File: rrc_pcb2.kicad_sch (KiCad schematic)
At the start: 15 parts, among them J1 Conn_01x02_Male-Connector, J2 Conn_01x03_Male-Connector, J3 digital logic connection, U1 iridium9602, U2 Teensy4.1, U3 BN220-GPS, U4 ICM-20948, U5 MS5611, U6 logo, U7 voltReg

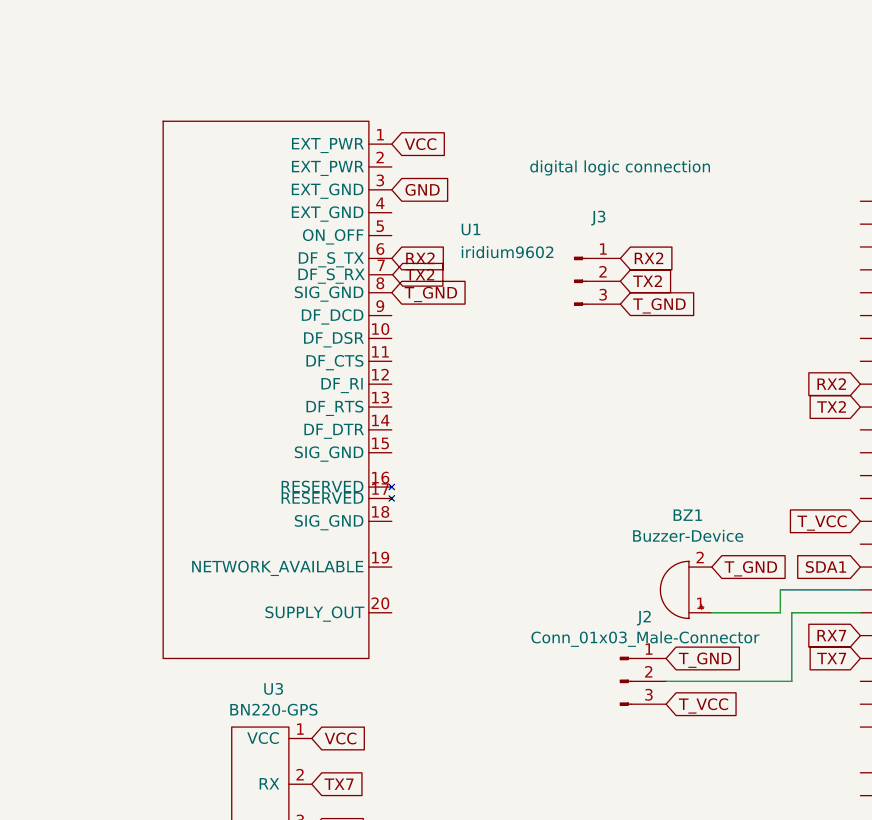
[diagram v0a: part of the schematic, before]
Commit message: tweaked srad main board
tweaked iridium footprints and volt reg footprints and added a back board just in case iridium doenst pan out; uses rfd900p instead.
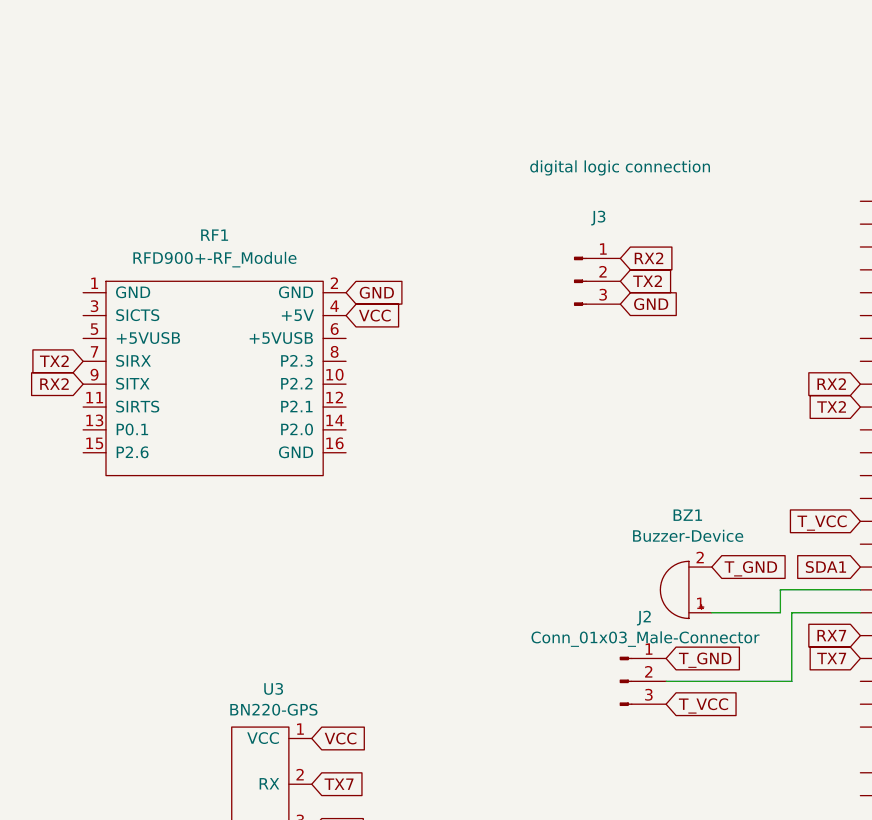
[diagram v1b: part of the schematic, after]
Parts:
- removed U1: iridium9602, iridium9602:iridium9602, symbol parts:iridium9602
- added RF1: RFD900+-RF_Module, rfd900+:RFD900+, symbol parts:RFD900+-RF_Module
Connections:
- net GND: now also J3.3 (Pin_3), RF1.2 (GND)
- net RX2: now also RF1.9 (SITX)
- net TX2: now also RF1.7 (SIRX)
- net T_GND: no longer J3.3 (Pin_3)
- net VCC: now also RF1.4 (+5V)
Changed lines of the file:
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@@
+    )
+  )
+  (global_label "GND" (shape input) (at 72.39 33.02 0) (fields_autoplaced)
+    (effects (font (size 1.27 1.27)) (justify left))
+    (property "Intersheet References" "${INTERSHEET_REFS}" (id 0) (at 0 -68.58 0)
+      (effects (font (size 1.27 1.27)) hide)
     )
   )
@@
     )
   )
-  (global_label "TX2" (shape input) (at 47.0887 29.7566 0) (fields_autoplaced)
-    (effects (font (size 1.27 1.27)) (justify left))
-    (property "Intersheet References" "${INTERSHEET_REFS}" (id 0) (at 52.7996 29.6772 0)
-      (effects (font (size 1.27 1.27)) (justify left) hide)
+  (global_label "TX2" (shape input) (at 12.7 39.37 180) (fields_autoplaced)
+    (effects (font (size 1.27 1.27)) (justify right))
+    (property "Intersheet References" "${INTERSHEET_REFS}" (id 0) (at 6.9891 39.4494 0)
+      (effects (font (size 1.27 1.27)) (justify right) hide)
     )
   )
@@
     )
   )
-  (global_label "VCC" (shape input) (at 46.99 15.24 0) (fields_autoplaced)
-    (effects (font (size 1.27 1.27)) (justify left))
-    (property "Intersheet References" "${INTERSHEET_REFS}" (id 0) (at -121.92 -113.03 0)
+  (global_label "VCC" (shape input) (at 41.91 34.29 0) (fields_autoplaced)
+    (effects (font (size 1.27 1.27)) (justify left))
+    (property "Intersheet References" "${INTERSHEET_REFS}" (id 0) (at -127 -93.98 0)
       (effects (font (size 1.27 1.27)) hide)
     )
@@
     )
   )
-  (global_label "RX2" (shape input) (at 46.99 27.94 0) (fields_autoplaced)
-    (effects (font (size 1.27 1.27)) (justify left))
-    (property "Intersheet References" "${INTERSHEET_REFS}" (id 0) (at 53.0032 27.8606 0)
-      (effects (font (size 1.27 1.27)) (justify left) hide)
+  (global_label "RX2" (shape input) (at 12.7 41.91 180) (fields_autoplaced)
+    (effects (font (size 1.27 1.27)) (justify right))
+    (property "Intersheet References" "${INTERSHEET_REFS}" (id 0) (at 6.6868 41.9894 0)
+      (effects (font (size 1.27 1.27)) (justify right) hide)
     )
   )
@@
     )
   )
-  (global_label "T_GND" (shape input) (at 46.99 31.75 0) (fields_autoplaced)
-    (effects (font (size 1.27 1.27)) (justify left))
-    (property "Intersheet References" "${INTERSHEET_REFS}" (id 0) (at -19.05 -13.97 0)
-      (effects (font (size 1.27 1.27)) hide)
-    )
-  )
   (global_label "T_GND" (shape input) (at 38.1 95.25 0) (fields_autoplaced)
     (effects (font (size 1.27 1.27)) (justify left))
@@
     )
   )
-  (global_label "T_GND" (shape input) (at 72.39 33.02 0) (fields_autoplaced)
-    (effects (font (size 1.27 1.27)) (justify left))
-    (property "Intersheet References" "${INTERSHEET_REFS}" (id 0) (at 6.35 -12.7 0)
-      (effects (font (size 1.27 1.27)) hide)
-    )
-  )
   (global_label "VCC" (shape input) (at 38.1 81.28 0) (fields_autoplaced)
     (effects (font (size 1.27 1.27)) (justify left))
@@
     )
   )
-  (global_label "GND" (shape input) (at 46.99 20.32 0) (fields_autoplaced)
-    (effects (font (size 1.27 1.27)) (justify left))
-    (property "Intersheet References" "${INTERSHEET_REFS}" (id 0) (at -25.4 -81.28 0)
+  (global_label "GND" (shape input) (at 41.91 31.75 0) (fields_autoplaced)
+    (effects (font (size 1.27 1.27)) (justify left))
+    (property "Intersheet References" "${INTERSHEET_REFS}" (id 0) (at -30.48 -69.85 0)
       (effects (font (size 1.27 1.27)) hide)
     )
@@
     (pin "23")
     (pin "24")
-    (pin "3")
-    (pin "4")
-    (pin "5")
-    (pin "6")
-    (pin "7")
-    (pin "8")
-    (pin "9")
-  )
-  (symbol (lib_id "parts:iridium9602") (at 34.29 21.59 0) (unit 1)
-    (in_bom yes) (on_board yes) (fields_autoplaced)
-    (property "Reference" "U1" (id 0) (at 54.61 24.7649 0)
-      (effects (font (size 1.27 1.27)) (justify left))
-    )
-    (property "Value" "iridium9602" (id 1) (at 54.61 27.3049 0)
-      (effects (font (size 1.27 1.27)) (justify left))
-    )
-    (property "Footprint" "iridium9602:iridium9602" (id 2) (at 34.29 21.59 0)
-      (effects (font (size 1.27 1.27)) hide)
-    )
-    (property "Datasheet" "" (id 3) (at 34.29 21.59 0)
-      (effects (font (size 1.27 1.27)) hide)
-    )
-    (pin "1")
-    (pin "10")
-    (pin "11")
-    (pin "12")
-    (pin "13")
-    (pin "14")
-    (pin "15")
-    (pin "16")
-    (pin "17")
-    (pin "18")
-    (pin "19")
-    (pin "2")
-    (pin "20")
     (pin "3")
     (pin "4")
@@
     (pin "4")
   )
+  (symbol (lib_id "parts:RFD900+-RF_Module") (at 19.05 31.75 0) (unit 1)
+    (in_bom yes) (on_board yes) (fields_autoplaced)
+    (property "Reference" "RF1" (id 0) (at 27.305 25.4 0))
+    (property "Value" "RFD900+-RF_Module" (id 1) (at 27.305 27.94 0))
+    (property "Footprint" "rfd900+:RFD900+" (id 2) (at 19.05 31.75 0)
+      (effects (font (size 1.27 1.27)) hide)
+    )
+    (property "Datasheet" "" (id 3) (at 19.05 31.75 0)
+      (effects (font (size 1.27 1.27)) hide)
+    )
+    (pin "1")
+    (pin "10")
+    (pin "11")
+    (pin "12")
+    (pin "13")
+    (pin "14")
+    (pin "15")
+    (pin "16")
+    (pin "2")
+    (pin "3")
+    (pin "4")
+    (pin "5")
+    (pin "6")
+    (pin "7")
+    (pin "8")
+    (pin "9")
+  )
   (sheet_instances
     (path "/" (page "1"))
@@
       (reference "R4") (unit 1) (value "R-Device") (footprint "Resistor_THT:R_Axial_DIN0207_L6.3mm_D2.5mm_P10.16mm_Horizontal")
     )
-    (path "/84f80ca1-29d4-4e34-8c20-e0b5bcec9cb7"
-      (reference "U1") (unit 1) (value "iridium9602") (footprint "iridium9602:iridium9602")
+    (path "/f8d3fd09-f76b-4951-941b-625c4e65f1c1"
+      (reference "RF1") (unit 1) (value "RFD900+-RF_Module") (footprint "rfd900+:RFD900+")
     )
     (path "/e2a4979b-162a-4acf-966e-29cd5e9f5e0d"

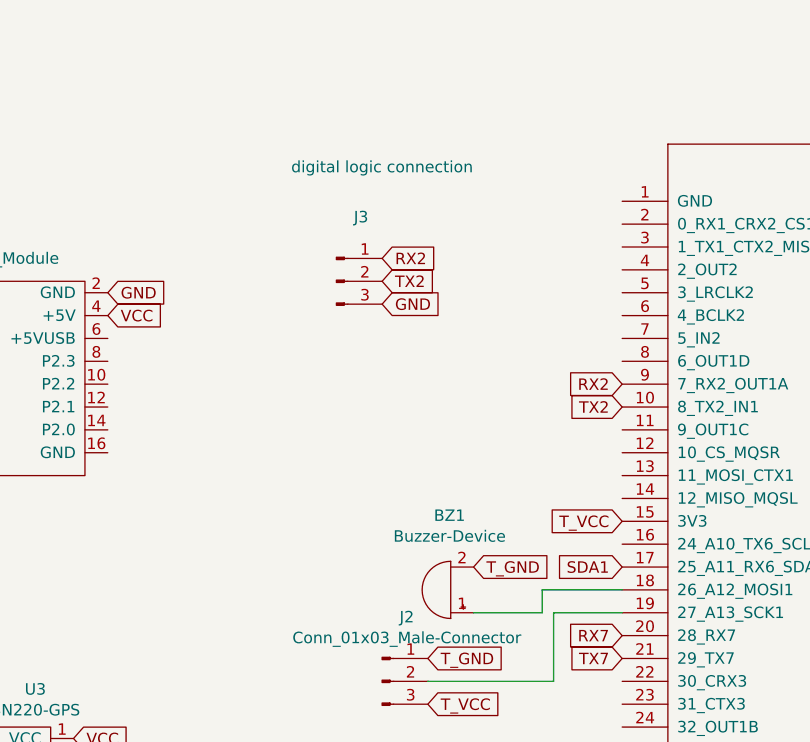
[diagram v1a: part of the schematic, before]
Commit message: fixed rfd traces
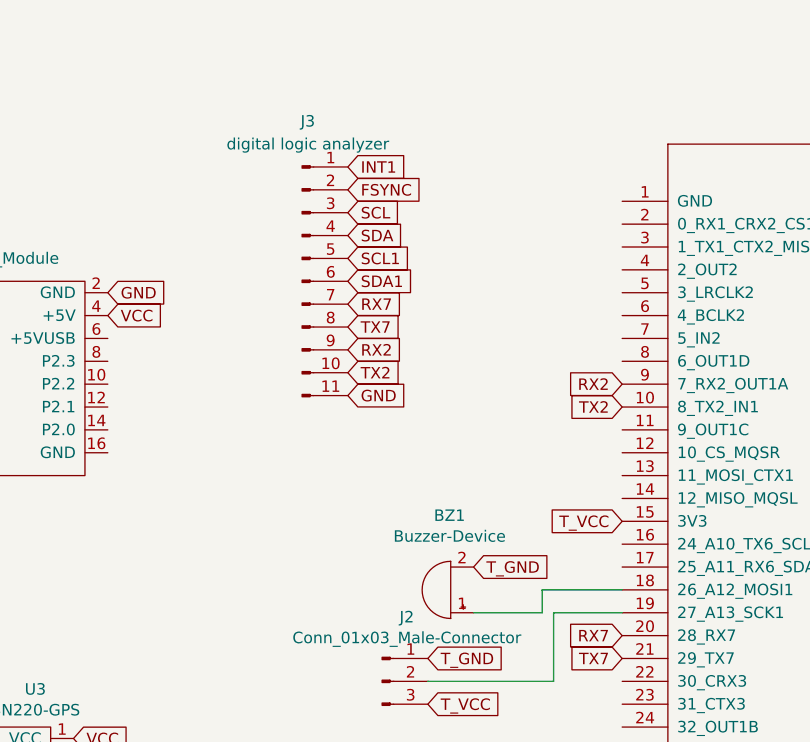
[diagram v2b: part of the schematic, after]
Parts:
- removed J3: digital logic connection, Connector_PinHeader_2.54mm:PinHeader_1x03_P2.54mm_Vertical, symbol rrc_pcb-rescue:Conn_01x03_Male-Connector
- added J3: digital logic analyzer, Connector_PinHeader_2.54mm:digital_logic_analyzer, symbol Connector:Conn_01x11_Male
- J2: footprint Connector_PinHeader_2.54mm:PinHeader_1x03_P2.54mm_Vertical -> Connector_PinHeader_2.54mm:PinHeader_1x11_P2.54mm_Vertical
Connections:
- net FSYNC: now also J3.2 (Pin_2)
- net GND: now also J3.11 (Pin_11)
- net INT1: now also J3.1 (Pin_1)
- net RX2: now also J3.9 (Pin_9)
- net RX7: now also J3.7 (Pin_7)
- net SCL: now also J3.3 (Pin_3)
- net SCL1: now also J3.5 (Pin_5)
- net SDA: now also J3.4 (Pin_4)
- net SDA1: now also J3.6 (Pin_6); no longer U2.17 (25_A11_RX6_SDA2)
- net TX2: now also J3.10 (Pin_10)
- net TX7: now also J3.8 (Pin_8)
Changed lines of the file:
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@@
+    )
+  )
+  (global_label "TX7" (shape input) (at 68.58 35.56 0) (fields_autoplaced)
+    (effects (font (size 1.27 1.27)) (justify left))
+    (property "Intersheet References" "${INTERSHEET_REFS}" (id 0) (at 74.2909 35.4806 0)
+      (effects (font (size 1.27 1.27)) (justify left) hide)
     )
   )
@@
     )
   )
+  (global_label "GND" (shape input) (at 68.58 43.18 0) (fields_autoplaced)
+    (effects (font (size 1.27 1.27)) (justify left))
+    (property "Intersheet References" "${INTERSHEET_REFS}" (id 0) (at -3.81 -58.42 0)
+      (effects (font (size 1.27 1.27)) hide)
+    )
+  )
+  (global_label "SDA" (shape input) (at 68.58 25.4 0) (fields_autoplaced)
+    (effects (font (size 1.27 1.27)) (justify left))
+    (property "Intersheet References" "${INTERSHEET_REFS}" (id 0) (at 74.4723 25.3206 0)
+      (effects (font (size 1.27 1.27)) (justify left) hide)
+    )
+  )
+  (global_label "FSYNC" (shape input) (at 68.58 20.32 0) (fields_autoplaced)
+    (effects (font (size 1.27 1.27)) (justify left))
+    (property "Intersheet References" "${INTERSHEET_REFS}" (id 0) (at 76.8913 20.3994 0)
+      (effects (font (size 1.27 1.27)) (justify left) hide)
+    )
+  )
   (global_label "T_GND" (shape input) (at 77.47 72.39 0) (fields_autoplaced)
     (effects (font (size 1.27 1.27)) (justify left))
@@
     )
   )
-  (global_label "GND" (shape input) (at 72.39 33.02 0) (fields_autoplaced)
-    (effects (font (size 1.27 1.27)) (justify left))
-    (property "Intersheet References" "${INTERSHEET_REFS}" (id 0) (at 0 -68.58 0)
-      (effects (font (size 1.27 1.27)) hide)
-    )
-  )
   (global_label "FSYNC" (shape input) (at 154.94 67.31 0) (fields_autoplaced)
     (effects (font (size 1.27 1.27)) (justify left))
@@
     )
   )
+  (global_label "SCL1" (shape input) (at 68.58 27.94 0) (fields_autoplaced)
+    (effects (font (size 1.27 1.27)) (justify left))
+    (property "Intersheet References" "${INTERSHEET_REFS}" (id 0) (at 75.6213 28.0194 0)
+      (effects (font (size 1.27 1.27)) (justify left) hide)
+    )
+  )
   (global_label "SCL1" (shape input) (at 154.94 46.99 0) (fields_autoplaced)
     (effects (font (size 1.27 1.27)) (justify left))
@@
     )
   )
-  (global_label "SDA1" (shape input) (at 99.06 62.23 180) (fields_autoplaced)
-    (effects (font (size 1.27 1.27)) (justify right))
-    (property "Intersheet References" "${INTERSHEET_REFS}" (id 0) (at 91.9582 62.3094 0)
-      (effects (font (size 1.27 1.27)) (justify right) hide)
-    )
-  )
   (global_label "INT1" (shape input) (at 222.25 49.53 180) (fields_autoplaced)
     (effects (font (size 1.27 1.27)) (justify right))
@@
     )
   )
+  (global_label "RX7" (shape input) (at 68.58 33.02 0) (fields_autoplaced)
+    (effects (font (size 1.27 1.27)) (justify left))
+    (property "Intersheet References" "${INTERSHEET_REFS}" (id 0) (at 74.5932 32.9406 0)
+      (effects (font (size 1.27 1.27)) (justify left) hide)
+    )
+  )
   (global_label "T_GND" (shape input) (at 38.1 95.25 0) (fields_autoplaced)
     (effects (font (size 1.27 1.27)) (justify left))
@@
     )
   )
+  (global_label "SCL" (shape input) (at 68.58 22.86 0) (fields_autoplaced)
+    (effects (font (size 1.27 1.27)) (justify left))
+    (property "Intersheet References" "${INTERSHEET_REFS}" (id 0) (at 74.4118 22.7806 0)
+      (effects (font (size 1.27 1.27)) (justify left) hide)
+    )
+  )
   (global_label "VCC" (shape input) (at 38.1 81.28 0) (fields_autoplaced)
     (effects (font (size 1.27 1.27)) (justify left))
@@
     )
   )
+  (global_label "TX2" (shape input) (at 68.58 40.64 0) (fields_autoplaced)
+    (effects (font (size 1.27 1.27)) (justify left))
+    (property "Intersheet References" "${INTERSHEET_REFS}" (id 0) (at 74.2909 40.5606 0)
+      (effects (font (size 1.27 1.27)) (justify left) hide)
+    )
+  )
   (global_label "T_GND" (shape input) (at 241.3 100.33 180) (fields_autoplaced)
     (effects (font (size 1.27 1.27)) (justify right))
@@
     )
   )
+  (global_label "SDA1" (shape input) (at 68.58 30.48 0) (fields_autoplaced)
+    (effects (font (size 1.27 1.27)) (justify left))
+    (property "Intersheet References" "${INTERSHEET_REFS}" (id 0) (at 75.6818 30.4006 0)
+      (effects (font (size 1.27 1.27)) (justify left) hide)
+    )
+  )
   (global_label "T_VCC" (shape input) (at 222.25 102.87 180) (fields_autoplaced)
     (effects (font (size 1.27 1.27)) (justify right))
@@
     )
   )
+  (global_label "RX2" (shape input) (at 68.58 38.1 0) (fields_autoplaced)
+    (effects (font (size 1.27 1.27)) (justify left))
+    (property "Intersheet References" "${INTERSHEET_REFS}" (id 0) (at 74.5932 38.0206 0)
+      (effects (font (size 1.27 1.27)) (justify left) hide)
+    )
+  )
   (global_label "TX7" (shape input) (at 38.1 86.36 0) (fields_autoplaced)
     (effects (font (size 1.27 1.27)) (justify left))
@@
     )
   )
+  (global_label "INT1" (shape input) (at 68.58 17.78 0) (fields_autoplaced)
+    (effects (font (size 1.27 1.27)) (justify left))
+    (property "Intersheet References" "${INTERSHEET_REFS}" (id 0) (at 75.0166 17.7006 0)
+      (effects (font (size 1.27 1.27)) (justify left) hide)
+    )
+  )
   (global_label "VCC" (shape input) (at 261.62 11.43 0) (fields_autoplaced)
     (effects (font (size 1.27 1.27)) (justify left))
@@
     (effects (font (size 1.27 1.27)) (justify left))
     (property "Intersheet References" "${INTERSHEET_REFS}" (id 0) (at 180.2606 46.2382 90)
-      (effects (font (size 1.27 1.27)) (justify left) hide)
-    )
-  )
-  (global_label "RX2" (shape input) (at 72.39 27.94 0) (fields_autoplaced)
-    (effects (font (size 1.27 1.27)) (justify left))
-    (property "Intersheet References" "${INTERSHEET_REFS}" (id 0) (at 78.4032 27.8606 0)
-      (effects (font (size 1.27 1.27)) (justify left) hide)
-    )
-  )
-  (global_label "TX2" (shape input) (at 72.39 30.48 0) (fields_autoplaced)
-    (effects (font (size 1.27 1.27)) (justify left))
-    (property "Intersheet References" "${INTERSHEET_REFS}" (id 0) (at 78.1009 30.4006 0)
       (effects (font (size 1.27 1.27)) (justify left) hide)
     )
@@
     (property "Reference" "J2" (id 0) (at 75.1332 67.7926 0))
     (property "Value" "Conn_01x03_Male-Connector" (id 1) (at 75.1332 70.104 0))
-    (property "Footprint" "Connector_PinHeader_2.54mm:PinHeader_1x03_P2.54mm_Vertical" (id 2) (at 72.39 74.93 0)
+    (property "Footprint" "Connector_PinHeader_2.54mm:PinHeader_1x11_P2.54mm_Vertical" (id 2) (at 72.39 74.93 0)
       (effects (font (size 1.27 1.27)) hide)
     )
@@
     (pin "9")
   )
-  (symbol (lib_id "rrc_pcb-rescue:Conn_01x03_Male-Connector") (at 67.31 30.48 0) (unit 1)
-    (in_bom yes) (on_board yes)
-    (property "Reference" "J3" (id 0) (at 70.0532 23.3426 0))
-    (property "Value" "digital logic connection" (id 1) (at 72.39 17.78 0))
-    (property "Footprint" "Connector_PinHeader_2.54mm:PinHeader_1x03_P2.54mm_Vertical" (id 2) (at 67.31 30.48 0)
-      (effects (font (size 1.27 1.27)) hide)
-    )
-    (property "Datasheet" "~" (id 3) (at 67.31 30.48 0)
-      (effects (font (size 1.27 1.27)) hide)
-    )
-    (pin "1")
-    (pin "2")
-    (pin "3")
+  (symbol (lib_id "Connector:Conn_01x11_Male") (at 63.5 30.48 0) (unit 1)
+    (in_bom yes) (on_board yes) (fields_autoplaced)
+    (property "Reference" "J3" (id 0) (at 64.135 12.7 0))
+    (property "Value" "digital logic analyzer" (id 1) (at 64.135 15.24 0))
+    (property "Footprint" "Connector_PinHeader_2.54mm:digital_logic_analyzer" (id 2) (at 63.5 30.48 0)
+      (effects (font (size 1.27 1.27)) hide)
+    )
+    (property "Datasheet" "~" (id 3) (at 63.5 30.48 0)
+      (effects (font (size 1.27 1.27)) hide)
+    )
+    (pin "1")
+    (pin "10")
+    (pin "11")
+    (pin "2")
+    (pin "3")
+    (pin "4")
+    (pin "5")
+    (pin "6")
+    (pin "7")
+    (pin "8")
+    (pin "9")
   )
   (symbol (lib_id "teensy:Teensy4.1") (at 127 76.2 0) (unit 1)
@@
     )
     (path "/00000000-0000-0000-0000-000060f65d90"
-      (reference "J2") (unit 1) (value "Conn_01x03_Male-Connector") (footprint "Connector_PinHeader_2.54mm:PinHeader_1x03_P2.54mm_Vertical")
-    )
-    (path "/bc66338f-5aaa-4ddc-8d91-b0d7cbbd6cfb"
-      (reference "J3") (unit 1) (value "digital logic connection") (footprint "Connector_PinHeader_2.54mm:PinHeader_1x03_P2.54mm_Vertical")
+      (reference "J2") (unit 1) (value "Conn_01x03_Male-Connector") (footprint "Connector_PinHeader_2.54mm:PinHeader_1x11_P2.54mm_Vertical")
+    )
+    (path "/c405110e-364b-4c80-9560-cc4a663f2957"
+      (reference "J3") (unit 1) (value "digital logic analyzer") (footprint "Connector_PinHeader_2.54mm:digital_logic_analyzer")
     )
     (path "/00000000-0000-0000-0000-000060f42e96"
